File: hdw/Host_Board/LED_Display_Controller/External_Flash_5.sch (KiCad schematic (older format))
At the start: 17 parts

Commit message: I said never do this, it's bad for you
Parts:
- removed J?: WP5, symbol Connector_Generic:Conn_02x01
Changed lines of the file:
@@
 $Descr A 11000 8500
 encoding utf-8
-Sheet 18 32
+Sheet 17 31
 Title ""
 Date ""
@@
 F 3 "" H 6080 4050 50  0001 C CNN
 	1    6080 4050
-	1    0    0    -1
-$EndComp
-$Comp
-L Custom_Library:+3.3V #PWR?
-U 1 1 5BBE964B
-P 6080 3250
-F 0 "#PWR?" H 6080 3100 50  0001 C CNN
-F 1 "+3.3V" H 6080 3390 50  0000 C CNN
-F 2 "" H 6080 3250 50  0000 C CNN
-F 3 "" H 6080 3250 50  0000 C CNN
-	1    6080 3250
 	1    0    0    -1
 $EndComp
@@
 $EndComp
 $Comp
-L Custom_Library:+3.3V #PWR?
-U 1 1 5BBE96A5
-P 5110 2980
-F 0 "#PWR?" H 5110 2830 50  0001 C CNN
-F 1 "+3.3V" H 5110 3120 50  0000 C CNN
-F 2 "" H 5110 2980 50  0000 C CNN
-F 3 "" H 5110 2980 50  0000 C CNN
-	1    5110 2980
-	1    0    0    -1
-$EndComp
-$Comp
-L Custom_Library:+3.3V #PWR?
-U 1 1 5BBE96AB
-P 4520 2980
-F 0 "#PWR?" H 4520 2830 50  0001 C CNN
-F 1 "+3.3V" H 4520 3120 50  0000 C CNN
-F 2 "" H 4520 2980 50  0000 C CNN
-F 3 "" H 4520 2980 50  0000 C CNN
-	1    4520 2980
-	1    0    0    -1
-$EndComp
-$Comp
-L Custom_Library:+3.3V #PWR?
-U 1 1 5BBE96B1
-P 3930 2980
-F 0 "#PWR?" H 3930 2830 50  0001 C CNN
-F 1 "+3.3V" H 3930 3120 50  0000 C CNN
-F 2 "" H 3930 2980 50  0000 C CNN
-F 3 "" H 3930 2980 50  0000 C CNN
-	1    3930 2980
-	1    0    0    -1
-$EndComp
-$Comp
 L Custom_Library:R_Custom R?
 U 1 1 5BBE96BB
@@
 Wire Wire Line
 	3930 3650 5680 3650
-$Comp
-L Connector_Generic:Conn_02x01 J?
-U 1 1 5BBE96D2
-P 3930 4170
-AR Path="/5BB2595E/5BBE96D2" Ref="J?"  Part="1"
-AR Path="/5BB25AF0/5BBE96D2" Ref="J?"  Part="1"
-F 0 "J?" H 3980 4270 50  0000 C CNN
-F 1 "WP5" H 3980 4070 50  0000 C CNN
-F 2 "" H 3930 4170 50  0001 C CNN
-F 3 "~" H 3930 4170 50  0001 C CNN
-	1    3930 4170
-	0    1    1    0
-$EndComp
-Wire Wire Line
-	3930 3970 3930 3650
 Connection ~ 3930 3650
-$Comp
-L power:GND #PWR?
-U 1 1 5BBE96DB
-P 3930 4470
-F 0 "#PWR?" H 3930 4220 50  0001 C CNN
-F 1 "GND" H 3930 4320 50  0000 C CNN
-F 2 "" H 3930 4470 50  0001 C CNN
-F 3 "" H 3930 4470 50  0001 C CNN
-	1    3930 4470
-	1    0    0    -1
-$EndComp
 Text GLabel 3270 3450 0    50   Input ~ 0
 FLASH_MOSI
@@
 Text GLabel 3270 3650 0    40   Input ~ 0
 ~FLASH_WP5
+$Comp
+L power:+3.3V #PWR?
+U 1 1 5BDF94D1
+P 3930 2980
+F 0 "#PWR?" H 3930 2830 50  0001 C CNN
+F 1 "+3.3V" H 3930 3120 50  0000 C CNN
+F 2 "" H 3930 2980 50  0001 C CNN
+F 3 "" H 3930 2980 50  0001 C CNN
+	1    3930 2980
+	1    0    0    -1
+$EndComp
+$Comp
+L power:+3.3V #PWR?
+U 1 1 5BDF9505
+P 4520 2980
+F 0 "#PWR?" H 4520 2830 50  0001 C CNN
+F 1 "+3.3V" H 4520 3120 50  0000 C CNN
+F 2 "" H 4520 2980 50  0001 C CNN
+F 3 "" H 4520 2980 50  0001 C CNN
+	1    4520 2980
+	1    0    0    -1
+$EndComp
+$Comp
+L power:+3.3V #PWR?
+U 1 1 5BDF9532
+P 5110 2980
+F 0 "#PWR?" H 5110 2830 50  0001 C CNN
+F 1 "+3.3V" H 5110 3120 50  0000 C CNN
+F 2 "" H 5110 2980 50  0001 C CNN
+F 3 "" H 5110 2980 50  0001 C CNN
+	1    5110 2980
+	1    0    0    -1
+$EndComp
+$Comp
+L power:+3.3V #PWR?
+U 1 1 5BDF955F
+P 6080 3250
+F 0 "#PWR?" H 6080 3100 50  0001 C CNN
+F 1 "+3.3V" H 6080 3390 50  0000 C CNN
+F 2 "" H 6080 3250 50  0001 C CNN
+F 3 "" H 6080 3250 50  0001 C CNN
+	1    6080 3250
+	1    0    0    -1
+$EndComp
 $EndSCHEMATC

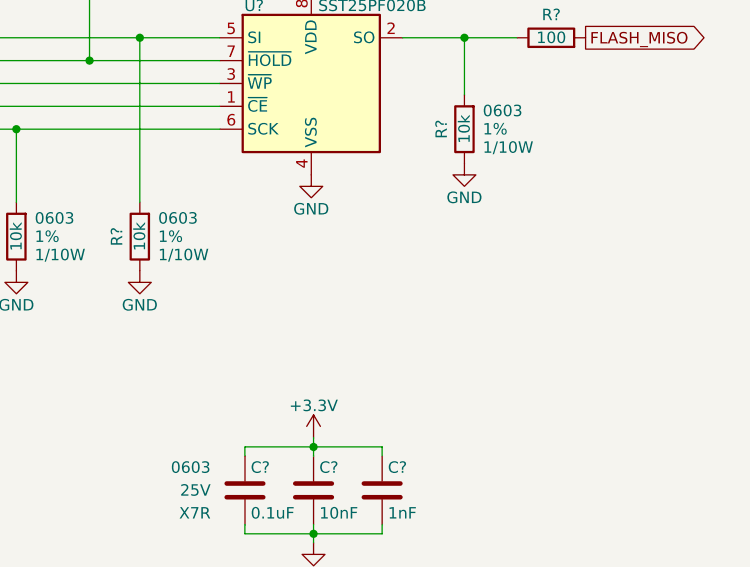
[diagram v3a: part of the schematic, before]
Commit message: Added graphical symbols to certain sheets
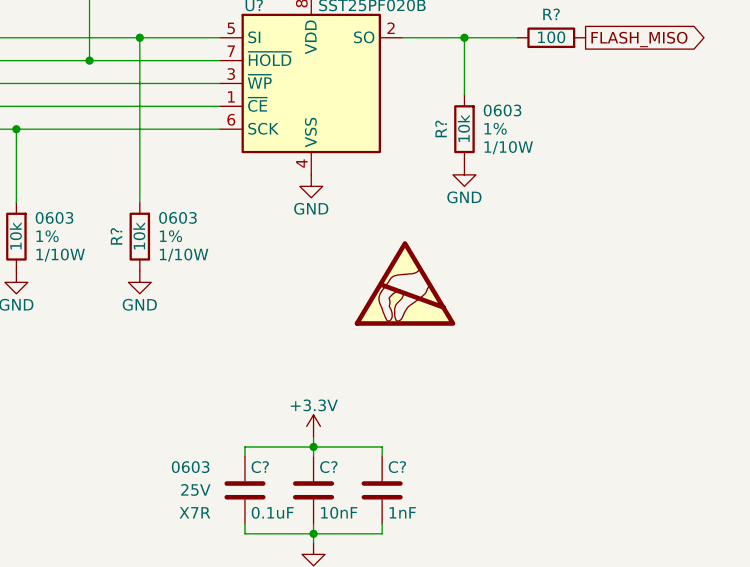
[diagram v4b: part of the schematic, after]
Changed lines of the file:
@@
+	1    0    0    -1
+$EndComp
+$Comp
+L Graphic:SYM_ESD_Large #SYM?
+U 1 1 5C029E51
+P 6490 4500
+AR Path="/5BAAE0FA/5C029E51" Ref="#SYM?"  Part="1"
+AR Path="/5BB182B1/5C029E51" Ref="#SYM?"  Part="1"
+F 0 "#SYM?" H 6490 4700 50  0001 C CNN
+F 1 "SYM_ESD_Large" H 6490 4250 50  0001 C CNN
+F 2 "" H 6485 4470 50  0001 C CNN
+F 3 "~" H 6485 4470 50  0001 C CNN
+	1    6490 4500
 	1    0    0    -1
 $EndComp

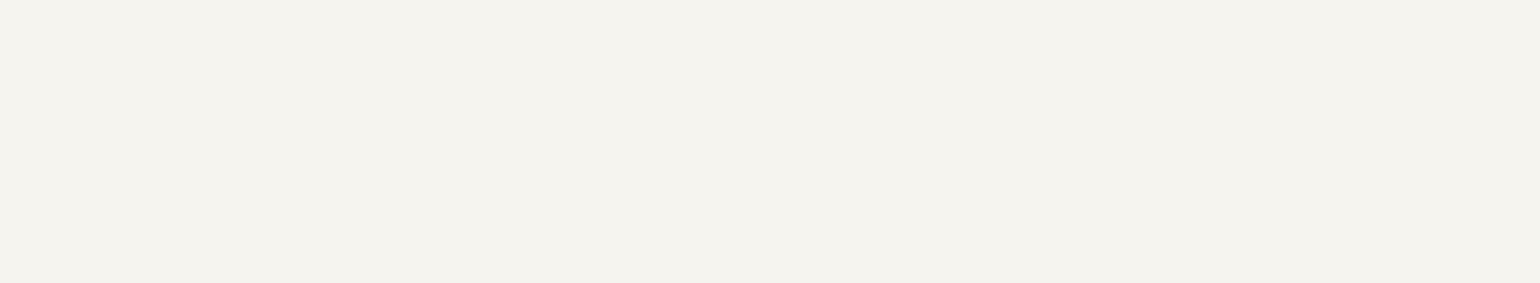
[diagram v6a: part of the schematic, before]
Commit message: Added titles and MU logo to each sheet
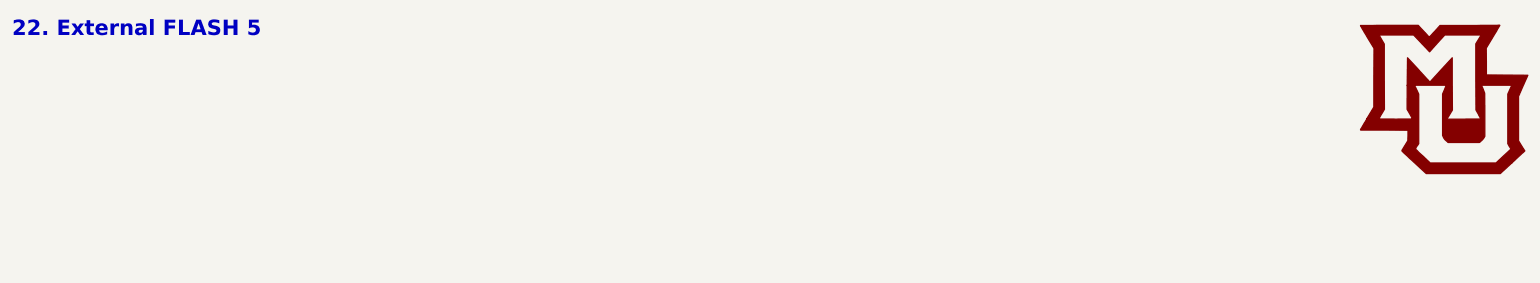
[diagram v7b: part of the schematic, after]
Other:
- note added: "22. External FLASH 5"
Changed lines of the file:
@@
+	1    0    0    -1
+$EndComp
+Text Notes 550  700  0    100  ~ 20
+22. External FLASH 5
+$Comp
+L LED_Display_Local_Library:MU_Logo #G?
+U 1 1 5BFFDE40
+P 9900 1100
+F 0 "#G?" H 9900 614 60  0001 C CNN
+F 1 "MU_Logo" H 9900 1586 60  0001 C CNN
+F 2 "" H 9900 1100 50  0001 C CNN
+F 3 "" H 9900 1100 50  0001 C CNN
+	1    9900 1100
 	1    0    0    -1
 $EndComp
